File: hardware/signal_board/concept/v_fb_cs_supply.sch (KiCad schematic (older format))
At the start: 12 parts, among them Q22 Q_NMOS_GDS, U19 LM358

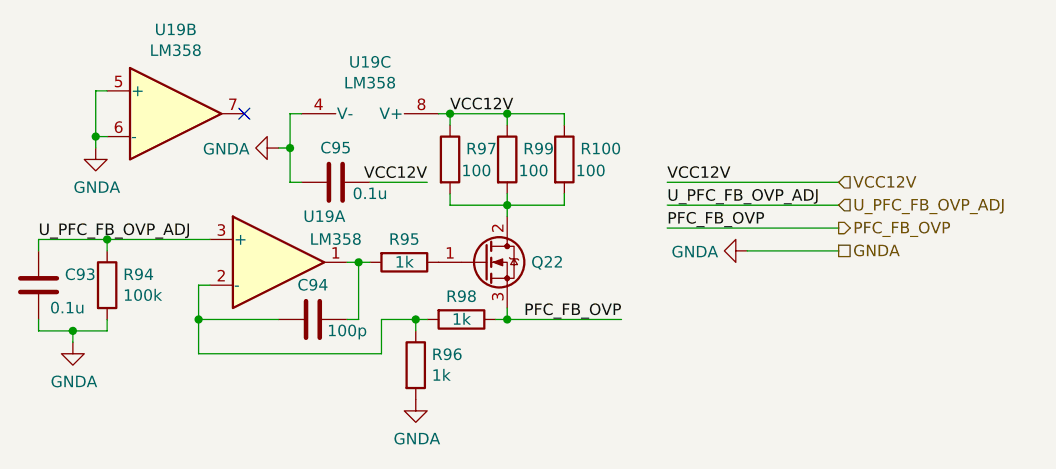
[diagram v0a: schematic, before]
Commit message: Add priduction board
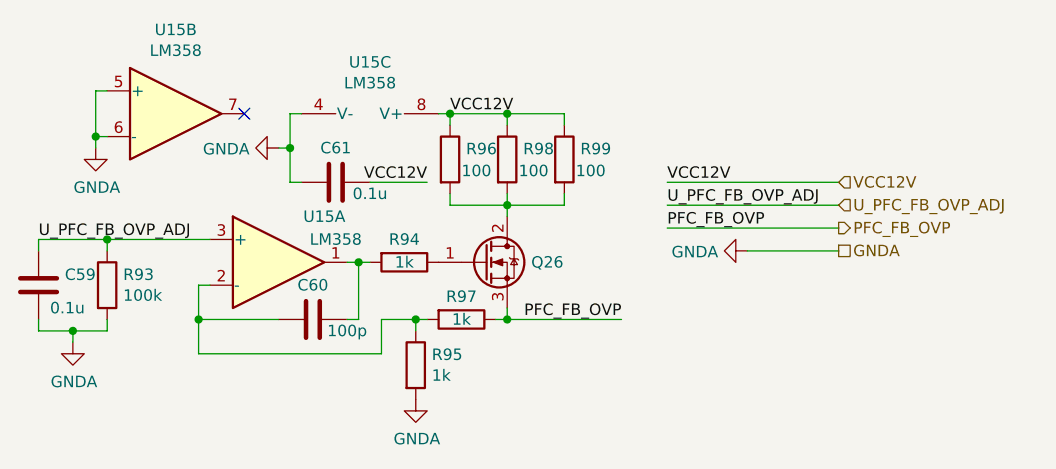
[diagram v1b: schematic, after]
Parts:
- renumbered C93 to C59, C94 to C60, C95 to C61, Q22 to Q26, R94 to R93, R95 to R94, R96 to R95, R97 to R96, R98 to R97, R99 to R98, R100 to R99, U19 to U15
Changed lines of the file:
@@
 $Descr A4 11693 8268
 encoding utf-8
-Sheet 7 12
+Sheet 10 16
 Title ""
 Date ""
@@
 $EndDescr
 $Comp
-L Amplifier_Operational:LM358 U19
+L Amplifier_Operational:LM358 U15
 U 1 1 5E4C8107
 P 4750 4100
-F 0 "U19" H 4950 4300 50  0000 C CNN
+F 0 "U15" H 4950 4300 50  0000 C CNN
 F 1 "LM358" H 5000 4200 50  0000 C CNN
 F 2 "Package_SO:SO-8_3.9x4.9mm_P1.27mm" H 4750 4100 50  0001 C CNN
@@
 $EndComp
 $Comp
-L Amplifier_Operational:LM358 U19
+L Amplifier_Operational:LM358 U15
 U 2 1 5E4C8C31
 P 4300 3450
-F 0 "U19" H 4300 3817 50  0000 C CNN
+F 0 "U15" H 4300 3817 50  0000 C CNN
 F 1 "LM358" H 4300 3726 50  0000 C CNN
 F 2 "Package_SO:SO-8_3.9x4.9mm_P1.27mm" H 4300 3450 50  0001 C CNN
@@
 $EndComp
 $Comp
-L Amplifier_Operational:LM358 U19
+L Amplifier_Operational:LM358 U15
 U 3 1 5E4C9B07
 P 5150 3550
-F 0 "U19" V 4825 3550 50  0000 C CNN
+F 0 "U15" V 4825 3550 50  0000 C CNN
 F 1 "LM358" V 4916 3550 50  0000 C CNN
 F 2 "Package_SO:SO-8_3.9x4.9mm_P1.27mm" H 5150 3550 50  0001 C CNN
@@
 NoConn ~ 4600 3450
 $Comp
-L Device:C C93
+L Device:C C59
 U 1 1 5E4CD95E
 P 3700 4200
-F 0 "C93" H 3815 4246 50  0000 L CNN
+F 0 "C59" H 3815 4246 50  0000 L CNN
 F 1 "0.1u" H 3750 4100 50  0000 L CNN
 F 2 "Capacitor_SMD:C_0603_1608Metric" H 3738 4050 50  0001 C CNN
@@
 $EndComp
 $Comp
-L Device:R R94
+L Device:R R93
 U 1 1 5E4CDDAB
 P 4000 4200
-F 0 "R94" H 4070 4246 50  0000 L CNN
+F 0 "R93" H 4070 4246 50  0000 L CNN
 F 1 "100k" H 4070 4155 50  0000 L CNN
 F 2 "Resistor_SMD:R_0603_1608Metric" V 3930 4200 50  0001 C CNN
@@
 $EndComp
 $Comp
-L power:GNDA #PWR072
+L power:GNDA #PWR065
 U 1 1 5E4CEF32
 P 3850 4450
-F 0 "#PWR072" H 3850 4200 50  0001 C CNN
+F 0 "#PWR065" H 3850 4200 50  0001 C CNN
 F 1 "GNDA" H 3855 4277 50  0000 C CNN
 F 2 "" H 3850 4450 50  0001 C CNN
@@
 $EndComp
 $Comp
-L power:GNDA #PWR073
+L power:GNDA #PWR066
 U 1 1 5E4CFB68
 P 3950 3600
-F 0 "#PWR073" H 3950 3350 50  0001 C CNN
+F 0 "#PWR066" H 3950 3350 50  0001 C CNN
 F 1 "GNDA" H 3955 3427 50  0000 C CNN
 F 2 "" H 3950 3600 50  0001 C CNN
@@
 Connection ~ 3950 3550
 $Comp
-L Device:C C94
+L Device:C C60
 U 1 1 5E4D18A4
 P 4900 4350
-F 0 "C94" V 4750 4350 50  0000 C CNN
+F 0 "C60" V 4750 4350 50  0000 C CNN
 F 1 "100p" V 4950 4500 50  0000 C CNN
 F 2 "Capacitor_SMD:C_0603_1608Metric" H 4938 4200 50  0001 C CNN
@@
 	5100 4100 5050 4100
 $Comp
-L Device:R R95
+L Device:R R94
 U 1 1 5E4D35D4
 P 5300 4100
-F 0 "R95" V 5200 4100 50  0000 C CNN
+F 0 "R94" V 5200 4100 50  0000 C CNN
 F 1 "1k" V 5300 4100 50  0000 C CNN
 F 2 "Resistor_SMD:R_0603_1608Metric" V 5230 4100 50  0001 C CNN
@@
 $EndComp
 $Comp
-L Device:Q_NMOS_GDS Q22
+L Device:Q_NMOS_GDS Q26
 U 1 1 5E4D45A1
 P 5650 4100
-F 0 "Q22" H 5855 4100 50  0000 L CNN
+F 0 "Q26" H 5855 4100 50  0000 L CNN
 F 1 "Q_NMOS_GDS" H 5854 4055 50  0001 L CNN
 F 2 "Package_TO_SOT_SMD:TO-252-2" H 5850 4200 50  0001 C CNN
@@
 Connection ~ 5100 4100
 $Comp
-L Device:R R99
+L Device:R R98
 U 1 1 5E4D644C
 P 5750 3650
-F 0 "R99" H 5820 3696 50  0000 L CNN
+F 0 "R98" H 5820 3696 50  0000 L CNN
 F 1 "100" H 5800 3600 50  0000 L CNN
 F 2 "Resistor_SMD:R_1206_3216Metric" V 5680 3650 50  0001 C CNN
@@
 $EndComp
 $Comp
-L Device:R R97
+L Device:R R96
 U 1 1 5E4D68B0
 P 5500 3650
-F 0 "R97" H 5570 3696 50  0000 L CNN
+F 0 "R96" H 5570 3696 50  0000 L CNN
 F 1 "100" H 5550 3600 50  0000 L CNN
 F 2 "Resistor_SMD:R_1206_3216Metric" V 5430 3650 50  0001 C CNN
@@
 $EndComp
 $Comp
-L Device:R R100
+L Device:R R99
 U 1 1 5E4D6C4F
 P 6000 3650
-F 0 "R100" H 6070 3696 50  0000 L CNN
+F 0 "R99" H 6070 3696 50  0000 L CNN
 F 1 "100" H 6050 3600 50  0000 L CNN
 F 2 "Resistor_SMD:R_1206_3216Metric" V 5930 3650 50  0001 C CNN
@@
 	5750 3450 6000 3450
 $Comp
-L Device:R R98
+L Device:R R97
 U 1 1 5E4D8897
 P 5550 4350
-F 0 "R98" V 5450 4350 50  0000 C CNN
+F 0 "R97" V 5450 4350 50  0000 C CNN
 F 1 "1k" V 5550 4350 50  0000 C CNN
 F 2 "Resistor_SMD:R_0603_1608Metric" V 5480 4350 50  0001 C CNN
@@
 $EndComp
 $Comp
-L Device:R R96
+L Device:R R95
 U 1 1 5E4D8D50
 P 5350 4550
-F 0 "R96" H 5420 4596 50  0000 L CNN
+F 0 "R95" H 5420 4596 50  0000 L CNN
 F 1 "1k" H 5420 4505 50  0000 L CNN
 F 2 "Resistor_SMD:R_0603_1608Metric" V 5280 4550 50  0001 C CNN
@@
 	5350 4350 5350 4400
 $Comp
-L power:GNDA #PWR075
+L power:GNDA #PWR068
 U 1 1 5E4D9D91
 P 5350 4700
-F 0 "#PWR075" H 5350 4450 50  0001 C CNN
+F 0 "#PWR068" H 5350 4450 50  0001 C CNN
 F 1 "GNDA" H 5355 4527 50  0000 C CNN
 F 2 "" H 5350 4700 50  0001 C CNN
@@
 Connection ~ 5500 3450
 $Comp
-L power:GNDA #PWR074
+L power:GNDA #PWR067
 U 1 1 5E4E55BB
 P 4750 3600
-F 0 "#PWR074" H 4750 3350 50  0001 C CNN
+F 0 "#PWR067" H 4750 3350 50  0001 C CNN
 F 1 "GNDA" V 4755 3473 50  0000 R CNN
 F 2 "" H 4750 3600 50  0001 C CNN
@@
 $EndComp
 $Comp
-L Device:C C95
+L Device:C C61
 U 1 1 5E4E5E24
 P 5000 3750
-F 0 "C95" V 4850 3750 50  0000 C CNN
+F 0 "C61" V 4850 3750 50  0000 C CNN
 F 1 "0.1u" V 5050 3900 50  0000 C CNN
 F 2 "Capacitor_SMD:C_0603_1608Metric" H 5038 3600 50  0001 C CNN
@@
 PFC_FB_OVP
 $Comp
-L power:GNDA #PWR076
+L power:GNDA #PWR069
 U 1 1 5E4F99EB
 P 6800 4050
-F 0 "#PWR076" H 6800 3800 50  0001 C CNN
+F 0 "#PWR069" H 6800 3800 50  0001 C CNN
 F 1 "GNDA" V 6805 3923 50  0000 R CNN
 F 2 "" H 6800 4050 50  0001 C CNN
